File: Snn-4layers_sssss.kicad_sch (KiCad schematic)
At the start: 78 parts, among them J1 Output connector, J2 Input connector, U1 ALD1106, U10 AP7366, U11 ADG619, U12 ADG619, U13 LTC6268xS8-10, U14 LT1715, U15 ADG619, U16 ADG619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

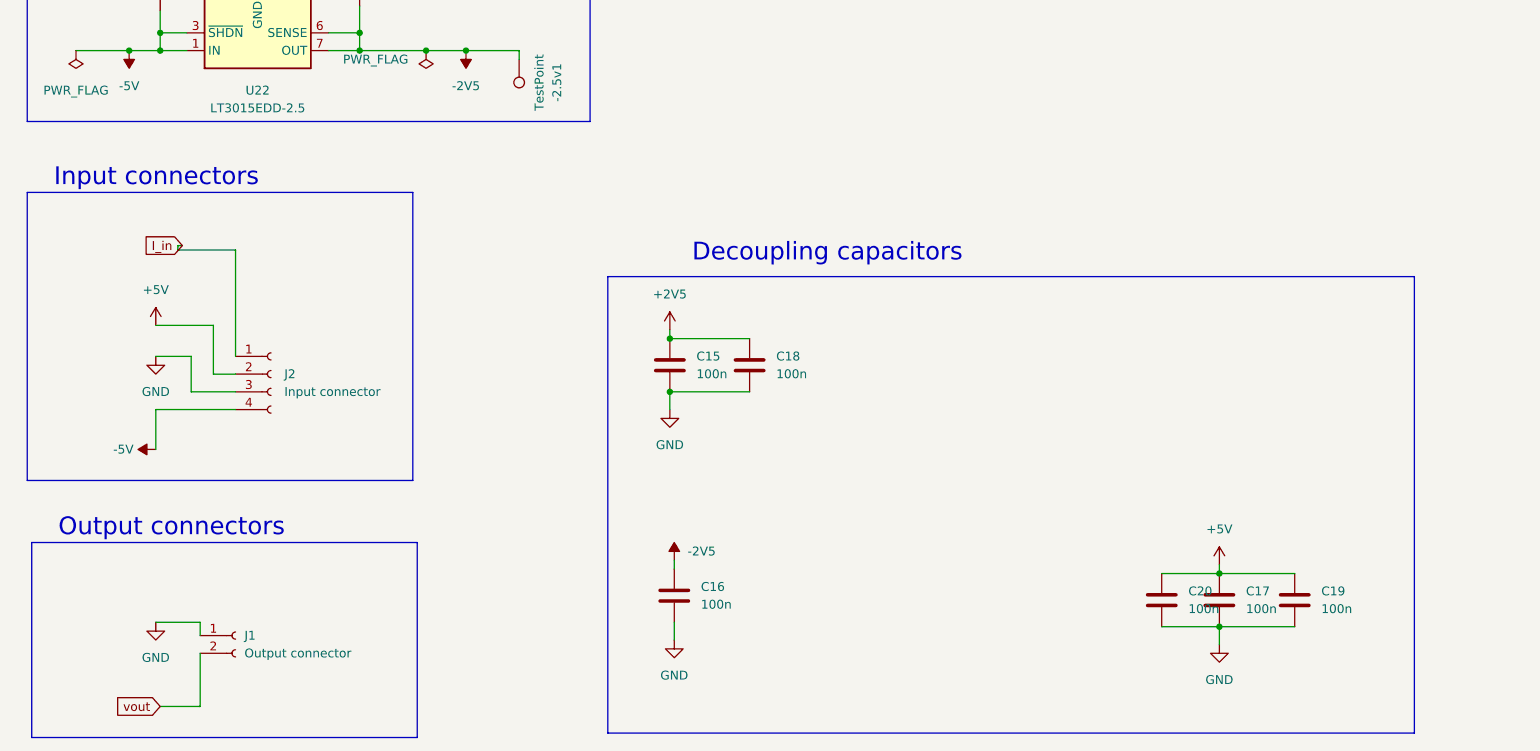
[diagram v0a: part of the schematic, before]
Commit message: added redundacy for the schematic
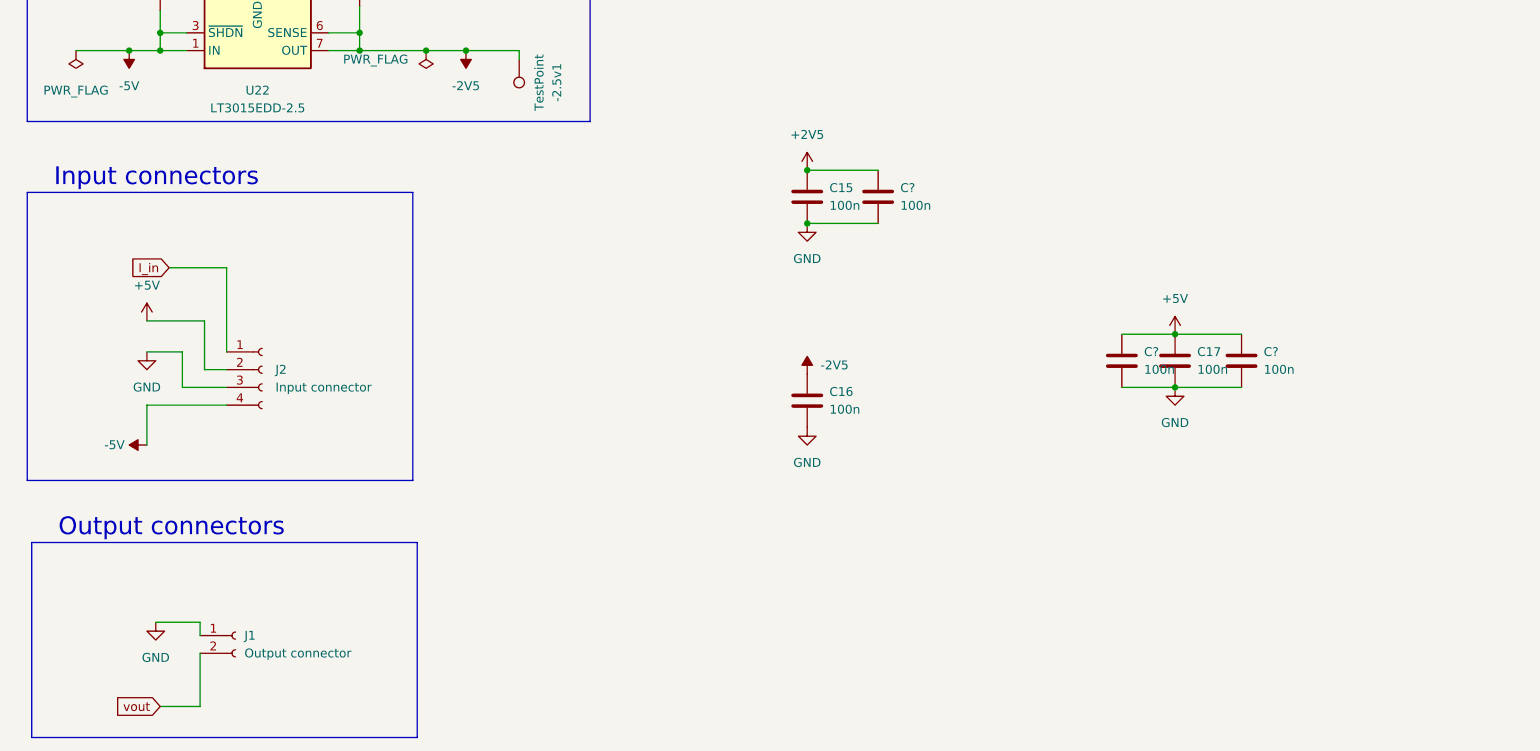
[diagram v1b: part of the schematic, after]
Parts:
- removed C18, C19, C20: 100n, Capacitor_SMD:C_0402_1005Metric, symbol Device:C
- added C? (x3): 100n, Capacitor_SMD:C_0402_1005Metric, symbol Device:C
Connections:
- net +2V5: now also C?.2
- net +5V: now also C?.2, C?.2
- net GND: now also C?.1, C?.1, C?.1
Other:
- note removed: "Decoupling capacitors"
- moved on the sheet: J2
